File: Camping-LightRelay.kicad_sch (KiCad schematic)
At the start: 57 parts, among them CN1 U262-061N-4BVC11, CN2 907-152A1022D10200, CN3 907-152A1022D10200, Q1 FDV301N, Q2 BC817, Q3 IRF7404, U1 USBLC6-2SC6, U2 CD4011UBM, U3 SI1865DDL, U4 ME2108A50M, U5 TLC555DTR

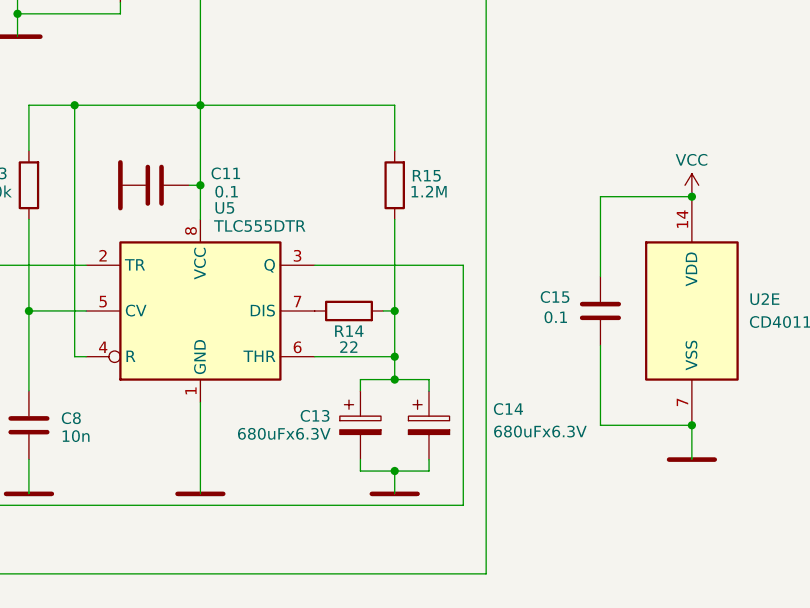
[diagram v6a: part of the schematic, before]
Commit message: Доделка ПП до финала
Проверка DRC, подгонка автоправил трассирования дорожек. Корректировка технических ограничений ПП. Расчет номиналов конденсаторов C11, C12.
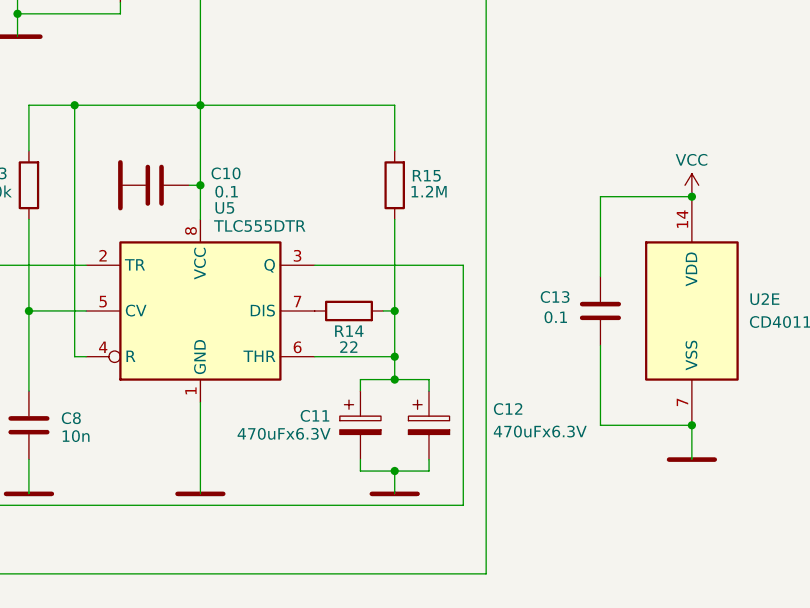
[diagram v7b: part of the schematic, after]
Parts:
- C11: renamed from C13; value 680uFx6.3V -> 470uFx6.3V; footprint Capacitor_Tantalum_SMD:CP_EIA-7343-43_Kemet-X_Pad2.25x2.55mm_HandSolder -> Capacitor_Tantalum_SMD:CP_EIA-7343-31_Kemet-D_Pad2.25x2.55mm_HandSolder; Part Number TPSE687K006R0045 -> TAJD477K006RNJ
- C12: renamed from C14; value 680uFx6.3V -> 470uFx6.3V; footprint Capacitor_Tantalum_SMD:CP_EIA-7343-43_Kemet-X_Pad2.25x2.55mm_HandSolder -> Capacitor_Tantalum_SMD:CP_EIA-7343-31_Kemet-D_Pad2.25x2.55mm_HandSolder; Part Number TPSE687K006R0045 -> TAJD477K006RNJ
- renumbered C11 to C10, C15 to C13
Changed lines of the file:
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@@
 		(dnp no)
 		(fields_autoplaced yes)
-		(property "Reference" "#PWR018"
+		(property "Reference" "#PWR017"
 			(at 236.22 91.44 0)
 			(effects
@@
 			(project "Camping-LightRelay"
 				(path "/5869d0d8-0214-47f7-a5b8-c2b5f6821b5d"
-					(reference "#PWR018")
+					(reference "#PWR017")
 					(unit 1)
 				)
@@
 		(dnp no)
 		(fields_autoplaced yes)
-		(property "Reference" "#PWR020"
+		(property "Reference" "#PWR019"
 			(at 254 151.13 0)
 			(effects
@@
 			(project "Camping-LightRelay"
 				(path "/5869d0d8-0214-47f7-a5b8-c2b5f6821b5d"
-					(reference "#PWR020")
+					(reference "#PWR019")
 					(unit 1)
 				)
@@
 		(on_board yes)
 		(dnp no)
-		(property "Reference" "C14"
+		(property "Reference" "C12"
 			(at 231.902 141.224 0)
 			(effects
@@
 			)
 		)
-		(property "Value" "680uFx6.3V"
+		(property "Value" "470uFx6.3V"
 			(at 231.902 142.24 0)
 			(effects
@@
 			)
 		)
-		(property "Footprint" "Capacitor_Tantalum_SMD:CP_EIA-7343-43_Kemet-X_Pad2.25x2.55mm_HandSolder"
+		(property "Footprint" "Capacitor_Tantalum_SMD:CP_EIA-7343-31_Kemet-D_Pad2.25x2.55mm_HandSolder"
 			(at 225.7552 146.05 0)
 			(effects
@@
 			)
 		)
-		(property "Description" "Polarized tantalum capacitor (type X)"
+		(property "Description" "Polarized tantalum capacitor (case D)"
 			(at 224.79 142.24 0)
 			(effects
@@
 			)
 		)
-		(property "Part Number" "TPSE687K006R0045"
+		(property "Part Number" "TAJD477K006RNJ"
 			(at 224.79 142.24 0)
 			(effects
@@
 			(project "Camping-LightRelay"
 				(path "/5869d0d8-0214-47f7-a5b8-c2b5f6821b5d"
-					(reference "C14")
+					(reference "C12")
 					(unit 1)
 				)
@@
 		(on_board yes)
 		(dnp no)
-		(property "Reference" "C15"
+		(property "Reference" "C13"
 			(at 240.538 128.778 0)
 			(effects
@@
 			(project "Camping-LightRelay"
 				(path "/5869d0d8-0214-47f7-a5b8-c2b5f6821b5d"
-					(reference "C15")
+					(reference "C13")
 					(unit 1)
 				)
@@
 		(on_board yes)
 		(dnp no)
-		(property "Reference" "#PWR017"
+		(property "Reference" "#PWR016"
 			(at 236.22 66.04 0)
 			(effects
@@
 			(project "Camping-LightRelay"
 				(path "/5869d0d8-0214-47f7-a5b8-c2b5f6821b5d"
-					(reference "#PWR017")
+					(reference "#PWR016")
 					(unit 1)
 				)
@@
 		(on_board yes)
 		(dnp no)
-		(property "Reference" "C11"
+		(property "Reference" "C10"
 			(at 203.962 114.3 90)
 			(effects
@@
 			(project "Camping-LightRelay"
 				(path "/5869d0d8-0214-47f7-a5b8-c2b5f6821b5d"
-					(reference "C11")
+					(reference "C10")
 					(unit 1)
 				)
@@
 		(on_board yes)
 		(dnp no)
-		(property "Reference" "#PWR015"
+		(property "Reference" "#PWR014"
 			(at 220.98 88.9 0)
 			(effects
@@
 			(project "Camping-LightRelay"
 				(path "/5869d0d8-0214-47f7-a5b8-c2b5f6821b5d"
-					(reference "#PWR015")
+					(reference "#PWR014")
 					(unit 1)
 				)
@@
 		(on_board yes)
 		(dnp no)
-		(property "Reference" "C13"
+		(property "Reference" "C11"
 			(at 213.868 141.986 0)
 			(effects
@@
 			)
 		)
-		(property "Value" "680uFx6.3V"
+		(property "Value" "470uFx6.3V"
 			(at 213.868 142.494 0)
 			(effects
@@
 			)
 		)
-		(property "Footprint" "Capacitor_Tantalum_SMD:CP_EIA-7343-43_Kemet-X_Pad2.25x2.55mm_HandSolder"
+		(property "Footprint" "Capacitor_Tantalum_SMD:CP_EIA-7343-31_Kemet-D_Pad2.25x2.55mm_HandSolder"
 			(at 218.1352 146.05 0)
 			(effects
@@
 			)
 		)
-		(property "Description" "Polarized tantalum capacitor (type X)"
+		(property "Description" "Polarized tantalum capacitor (case D)"
 			(at 217.17 142.24 0)
 			(effects
@@
 			)
 		)
-		(property "Part Number" "TPSE687K006R0045"
+		(property "Part Number" "TAJD477K006RNJ"
 			(at 217.17 142.24 0)
 			(effects
@@
 			(project "Camping-LightRelay"
 				(path "/5869d0d8-0214-47f7-a5b8-c2b5f6821b5d"
-					(reference "C13")
+					(reference "C11")
 					(unit 1)
 				)
@@
 		(dnp no)
 		(fields_autoplaced yes)
-		(property "Reference" "#PWR013"
+		(property "Reference" "#PWR012"
 			(at 195.58 115.57 0)
 			(effects
@@
 			(project "Camping-LightRelay"
 				(path "/5869d0d8-0214-47f7-a5b8-c2b5f6821b5d"
-					(reference "#PWR013")
+					(reference "#PWR012")
 					(unit 1)
 				)
@@
 		(dnp no)
 		(fields_autoplaced yes)
-		(property "Reference" "#PWR014"
+		(property "Reference" "#PWR013"
 			(at 199.39 154.94 0)
 			(effects
@@
 			(project "Camping-LightRelay"
 				(path "/5869d0d8-0214-47f7-a5b8-c2b5f6821b5d"
-					(reference "#PWR014")
+					(reference "#PWR013")
 					(unit 1)
 				)
@@
 		(on_board yes)
 		(dnp no)
-		(property "Reference" "#PWR019"
+		(property "Reference" "#PWR018"
 			(at 254 120.65 0)
 			(effects
@@
 			(project "Camping-LightRelay"
 				(path "/5869d0d8-0214-47f7-a5b8-c2b5f6821b5d"
-					(reference "#PWR019")
+					(reference "#PWR018")
 					(unit 1)
 				)
@@
 		(dnp no)
 		(fields_autoplaced yes)
-		(property "Reference" "#PWR016"
+		(property "Reference" "#PWR015"
 			(at 220.98 154.94 0)
 			(effects
@@
 			(project "Camping-LightRelay"
 				(path "/5869d0d8-0214-47f7-a5b8-c2b5f6821b5d"
-					(reference "#PWR016")
+					(reference "#PWR015")
 					(unit 1)
 				)

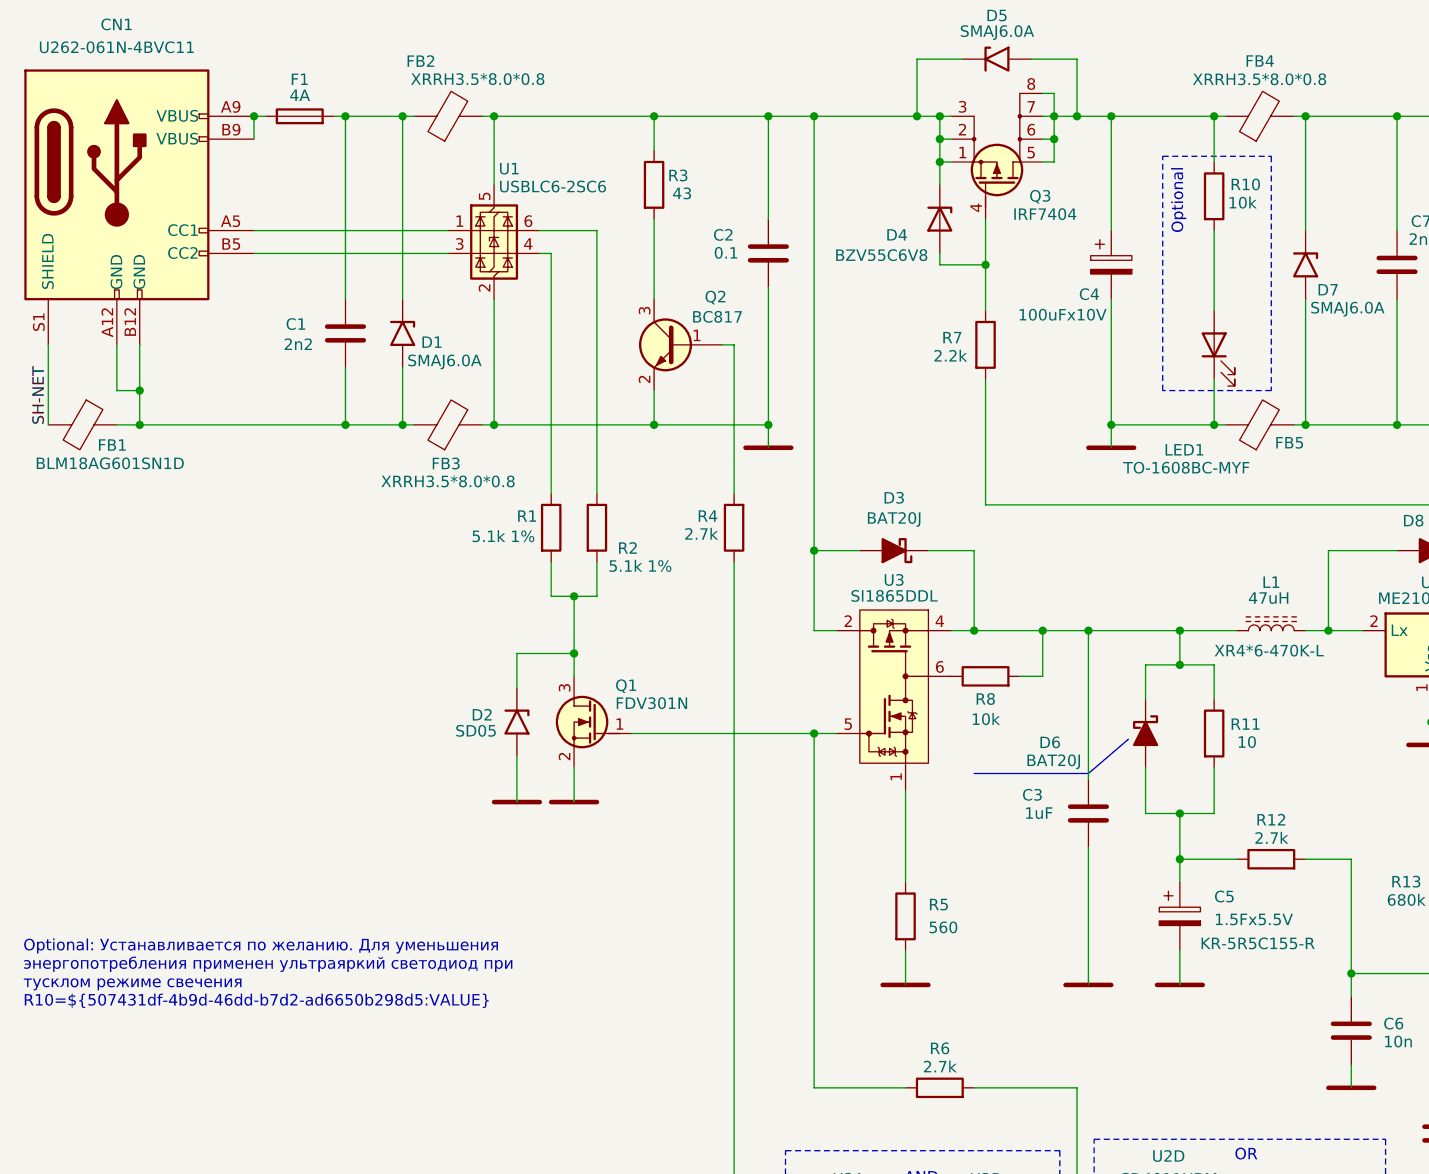
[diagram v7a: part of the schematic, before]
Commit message: Первая сборка production
Сборка всей конструкции и проверка на ПП, проверка работы
* Правка посадочного места ионистор C3 и печатной платы для него
* Замена D3 на обычный 1N4148 из-за утечек Шоттки
* Замена стабилитрона D4 на двойной TVS-диод, т.к. обнаружился обходной ток от внутреннего DC/DC преобразователя
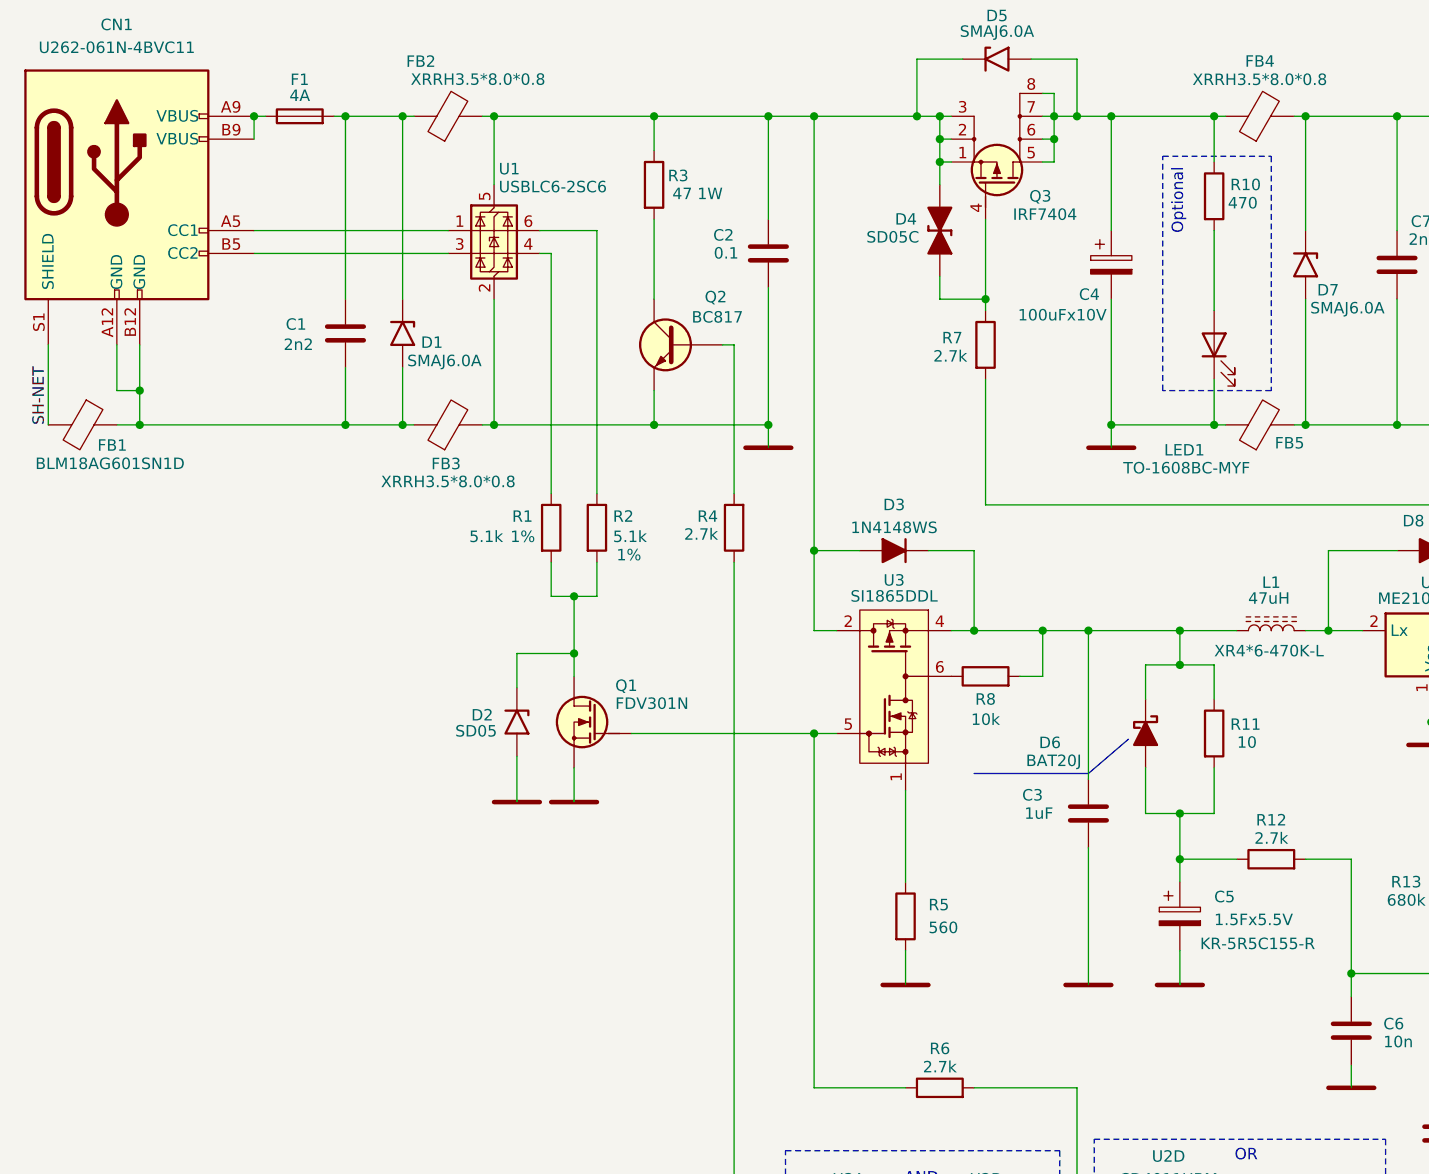
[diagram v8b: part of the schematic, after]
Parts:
- D3: value BAT20J -> 1N4148WS; symbol PCM_Diode_Schottky_AKL:BAT20J -> PCM_Diode_AKL:1N4148WS
- D4: value BZV55C6V8 -> SD05C; footprint Diode_SMD:D_MiniMELF -> Diode_SMD:D_SOD-323_HandSoldering; symbol Diode:BZV55C6V8 -> PCM_Diode_TVS_AKL:SD05C
- R1, R2: value 5.1k 1% -> 5.1k; Tolerance (none) -> 1%
- R10: value 10k -> 470
- R3: value 43 -> 47 1W; footprint Resistor_THT:R_Axial_DIN0309_L9.0mm_D3.2mm_P2.54mm_Vertical -> Resistor_THT:R_Axial_DIN0309_L9.0mm_D3.2mm_P5.08mm_Vertical
- R7: value 2.2k -> 2.7k
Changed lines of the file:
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@@
 	)
 	(junction
-		(at 129.54 45.72)
-		(diameter 0)
-		(color 0 0 0 0)
-	)
-	(junction
 		(at 139.7 153.67)
 		(diameter 0)
@@
 	)
 	(junction
+		(at 129.54 49.53)
+		(diameter 0)
+		(color 0 0 0 0)
+	)
+	(junction
 		(at 151.13 86.36)
 		(diameter 0)
@@
 	(wire
 		(pts
+			(xy 124.46 36.83) (xy 124.46 34.29)
+		)
+		(stroke
+			(width 0)
+			(type default)
+		)
+	)
+	(wire
+		(pts
 			(xy 135.89 29.21) (xy 137.16 29.21)
 		)
@@
 	(wire
 		(pts
-			(xy 124.46 34.29) (xy 124.46 36.83)
-		)
-		(stroke
-			(width 0)
-			(type default)
-		)
-	)
-	(wire
-		(pts
 			(xy 135.89 34.29) (xy 137.16 34.29)
 		)
@@
 	(wire
 		(pts
+			(xy 124.46 49.53) (xy 129.54 49.53)
+		)
+		(stroke
+			(width 0)
+			(type default)
+		)
+	)
+	(wire
+		(pts
 			(xy 81.28 44.45) (xy 81.28 71.12)
 		)
@@
 	(wire
 		(pts
-			(xy 134.62 22.86) (xy 139.7 22.86)
+			(xy 129.54 49.53) (xy 129.54 50.8)
 		)
 		(stroke
@@
 	(wire
 		(pts
-			(xy 151.13 106.68) (xy 154.94 106.68)
+			(xy 134.62 22.86) (xy 139.7 22.86)
 		)
 		(stroke
@@
 	(wire
 		(pts
-			(xy 101.6 156.21) (xy 106.68 156.21)
+			(xy 151.13 106.68) (xy 154.94 106.68)
 		)
 		(stroke
@@
 	(wire
 		(pts
-			(xy 139.7 137.16) (xy 139.7 153.67)
+			(xy 101.6 156.21) (xy 106.68 156.21)
 		)
 		(stroke
@@
 	(wire
 		(pts
-			(xy 133.35 91.44) (xy 135.89 91.44)
+			(xy 139.7 137.16) (xy 139.7 153.67)
 		)
 		(stroke
@@
 	(wire
 		(pts
-			(xy 236.22 69.85) (xy 238.76 69.85)
+			(xy 133.35 91.44) (xy 135.89 91.44)
 		)
 		(stroke
@@
 	(wire
 		(pts
-			(xy 110.49 86.36) (xy 110.49 77.47)
+			(xy 236.22 69.85) (xy 238.76 69.85)
 		)
 		(stroke
@@
 	(wire
 		(pts
-			(xy 92.71 40.64) (xy 92.71 49.53)
+			(xy 110.49 86.36) (xy 110.49 77.47)
 		)
 		(stroke
@@
 	(wire
 		(pts
-			(xy 129.54 40.64) (xy 129.54 45.72)
+			(xy 92.71 40.64) (xy 92.71 49.53)
 		)
 		(stroke
@@
 	(wire
 		(pts
-			(xy 33.02 63.5) (xy 35.56 63.5)
+			(xy 129.54 40.64) (xy 129.54 49.53)
 		)
 		(stroke
@@
 	(wire
 		(pts
-			(xy 129.54 45.72) (xy 124.46 45.72)
+			(xy 33.02 63.5) (xy 35.56 63.5)
 		)
 		(stroke
@@
 	(wire
 		(pts
-			(xy 124.46 45.72) (xy 124.46 44.45)
-		)
-		(stroke
-			(width 0)
-			(type default)
-		)
-	)
-	(wire
-		(pts
 			(xy 199.39 86.36) (xy 220.98 86.36)
 		)
@@
 	(wire
 		(pts
-			(xy 83.82 101.6) (xy 83.82 105.41)
+			(xy 124.46 49.53) (xy 124.46 46.99)
 		)
 		(stroke
@@
 	(wire
 		(pts
-			(xy 179.07 96.52) (xy 190.5 96.52)
+			(xy 83.82 101.6) (xy 83.82 105.41)
 		)
 		(stroke
@@
 	(wire
 		(pts
-			(xy 140.97 86.36) (xy 151.13 86.36)
+			(xy 179.07 96.52) (xy 190.5 96.52)
 		)
 		(stroke
@@
 	(wire
 		(pts
-			(xy 129.54 45.72) (xy 129.54 50.8)
+			(xy 140.97 86.36) (xy 151.13 86.36)
 		)
 		(stroke
@@
 		)
 	)
-	(text_box "\nOptional: Устанавливается по желанию. Для уменьшения энергопотребления применен ультраяркий светодиод при тусклом режиме свечения R10=${507431df-4b9d-46dd-b7d2-ad6650b298d5:VALUE} "
-		(exclude_from_sim yes)
-		(at 21.59 117.475 0)
-		(size 66.675 71.12)
-		(stroke
-			(width -0.0001)
-			(type default)
-		)
-		(fill
-			(type none)
-		)
-		(effects
-			(font
-				(size 1.27 1.27)
-			)
-			(justify left top)
-		)
-	)
 	(text "OR"
 		(exclude_from_sim no)
@@
 		(dnp no)
 		(property "Reference" "R2"
-			(at 88.646 77.978 0)
+			(at 88.138 74.422 0)
 			(effects
 				(font
@@
 			)
 		)
-		(property "Value" "5.1k 1%"
-			(at 87.63 78.486 0)
+		(property "Value" "5.1k"
+			(at 88.138 75.184 0)
 			(effects
 				(font
@@
 			)
 		)
+		(property "Tolerance" "1%"
+			(at 89.916 77.216 0)
+			(effects
+				(font
+					(size 1.27 1.27)
+				)
+				(justify top)
+			)
+		)
 		(pin "1"
 		)
@@
 	)
 	(symbol
-		(lib_id "Diode:BZV55C6V8")
-		(at 124.46 40.64 270)
+		(lib_id "PCM_Diode_TVS_AKL:SD05C")
+		(at 124.46 41.91 270)
 		(unit 1)
-		(exclude_from_sim yes)
+		(exclude_from_sim no)
 		(in_bom yes)
 		(on_board yes)
 		(dnp no)
 		(property "Reference" "D4"
-			(at 120.904 43.18 90)
+			(at 121.92 41.402 90)
 			(effects
 				(font
@@
 			)
 		)
-		(property "Value" "BZV55C6V8"
-			(at 123.19 43.942 90)
+		(property "Value" "SD05C"
+			(at 122.174 41.91 90)
 			(effects
 				(font
@@
 			)
 		)
-		(property "Footprint" "Diode_SMD:D_MiniMELF"
-			(at 120.015 40.64 0)
+		(property "Footprint" "Diode_SMD:D_SOD-323_HandSoldering"
+			(at 124.46 41.91 0)
 			(effects
 				(font
@@
 			)
 		)
-		(property "Datasheet" "https://assets.nexperia.com/documents/data-sheet/BZV55_SER.pdf"
-			(at 124.46 40.64 0)
+		(property "Datasheet" "https://www.tme.eu/Document/d78713adc390f06d220fb7a55d4c6ae5/sdxxc.pdf"
+			(at 124.46 41.91 0)
 			(effects
 				(font
@@
 			)
 		)
-		(property "Description" "6.8V, 500mW, 5%, Zener diode, MiniMELF"
-			(at 124.46 40.64 0)
+		(property "Description" "Bidirectional TVS Diode, 5V, 350W, Alternate KiCAD Library"
+			(at 124.46 41.91 0)
 			(effects
 				(font
@@
 			)
 		)
-		(property "Value" "10k"
+		(property "Value" "470"
 			(at 156.464 38.862 0)
 			(effects
@@
 			)
 		)
-		(property "Value" "2.2k"
+		(property "Value" "2.7k"
 			(at 127.508 55.88 0)
 			(effects
@@
 			)
 		)
-		(property "Value" "43"
+		(property "Value" "47 1W"
 			(at 94.742 37.084 0)
 			(effects
@@
 			)
 		)
-		(property "Footprint" "Resistor_THT:R_Axial_DIN0309_L9.0mm_D3.2mm_P2.54mm_Vertical"
+		(property "Footprint" "Resistor_THT:R_Axial_DIN0309_L9.0mm_D3.2mm_P5.08mm_Vertical"
 			(at 90.932 36.83 90)
 			(effects
@@
 		(dnp no)
 		(property "Reference" "R1"
-			(at 79.756 74.422 0)
+			(at 79.248 74.422 0)
 			(effects
 				(font
@@
 			)
 		)
-		(property "Value" "5.1k 1%"
-			(at 79.502 75.184 0)
+		(property "Value" "5.1k"
+			(at 75.946 75.184 0)
 			(effects
 				(font
@@
 			)
 		)
+		(property "Tolerance" "1%"
+			(at 79.502 75.184 0)
+			(effects
+				(font
+					(size 1.27 1.27)
+				)
+				(justify right top)
+			)
+		)
 		(pin "1"
 		)
@@
 	)
 	(symbol
-		(lib_id "PCM_Diode_Schottky_AKL:BAT20J")
+		(lib_id "PCM_Diode_AKL:1N4148WS")
 		(at 119.38 77.47 0)
 		(unit 1)
@@
 					(size 1.27 1.27)
 				)
-				(justify bottom)
 			)
 		)
-		(property "Value" "BAT20J"
-			(at 119.38 73.152 0)
+		(property "Value" "1N4148WS"
+			(at 119.38 74.93 0)
 			(effects
 				(font
 					(size 1.27 1.27)
 				)
-				(justify top)
 			)
 		)
@@
 			)
 		)
-		(property "Datasheet" "https://www.tme.eu/Document/0e41d40b03e8c95ae2fd8af27383fa23/BAT20J.pdf"
+		(property "Datasheet" "https://datasheet.octopart.com/1N4148WS-13-F-Diodes-Inc.-datasheet-11839050.pdf"
 			(at 119.38 77.47 0)
 			(effects
@@
 			)
 		)
-		(property "Description" "SOD-323 Schottky diode, 23V, 1A, Alternate KiCAD Library"
+		(property "Description" "SOD-323 Diode, Small Signal, Fast Switching, 75V, 150mA, 4ns, Alternate KiCad Library"
 			(at 119.38 77.47 0)
 			(effects
